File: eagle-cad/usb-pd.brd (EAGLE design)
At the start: 68.6 x 53.3 mm, 49 parts, among them Q1 CERAMIC_RESONATOR_SMD6M00G53Z, T1 FDN360P, U1 ATMEGA328-AU

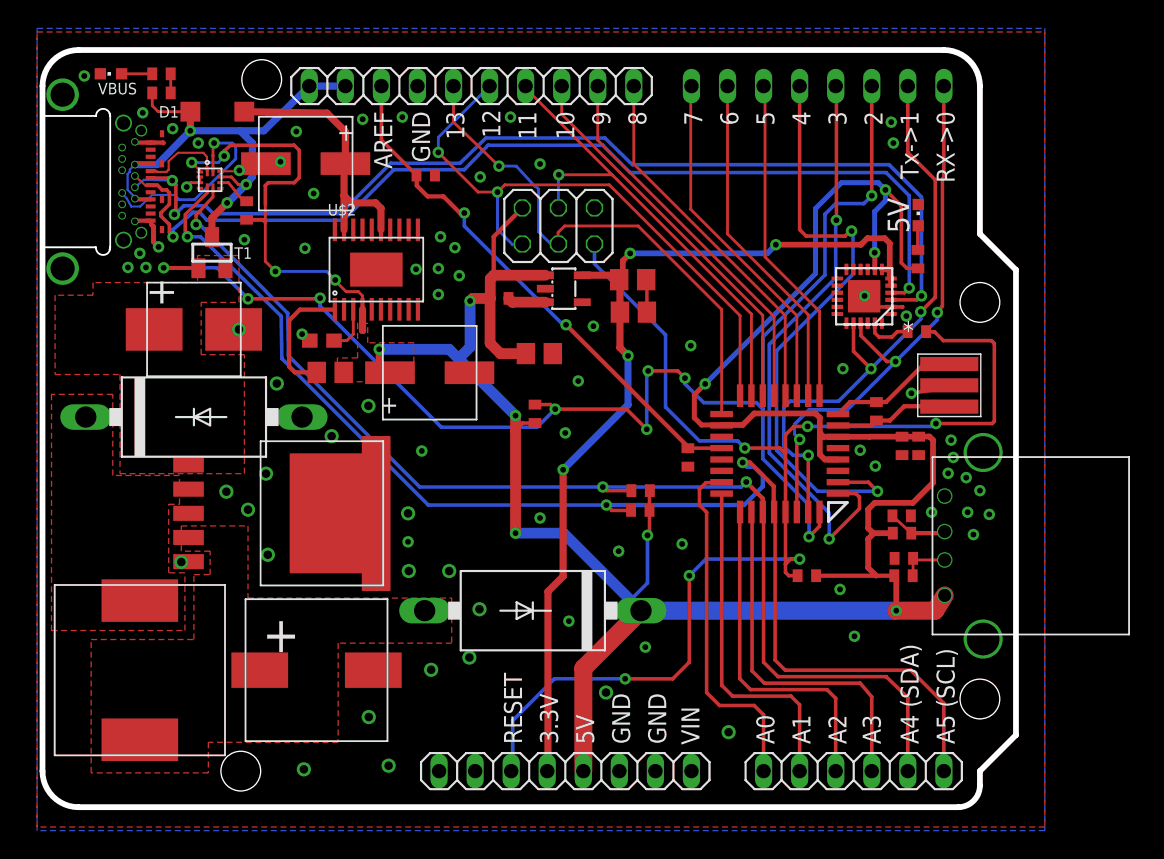
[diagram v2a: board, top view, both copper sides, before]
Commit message: Added new USB-C port, going to look at four-layer boards to get better Osh Park hole tolerances and ton of space for power planes
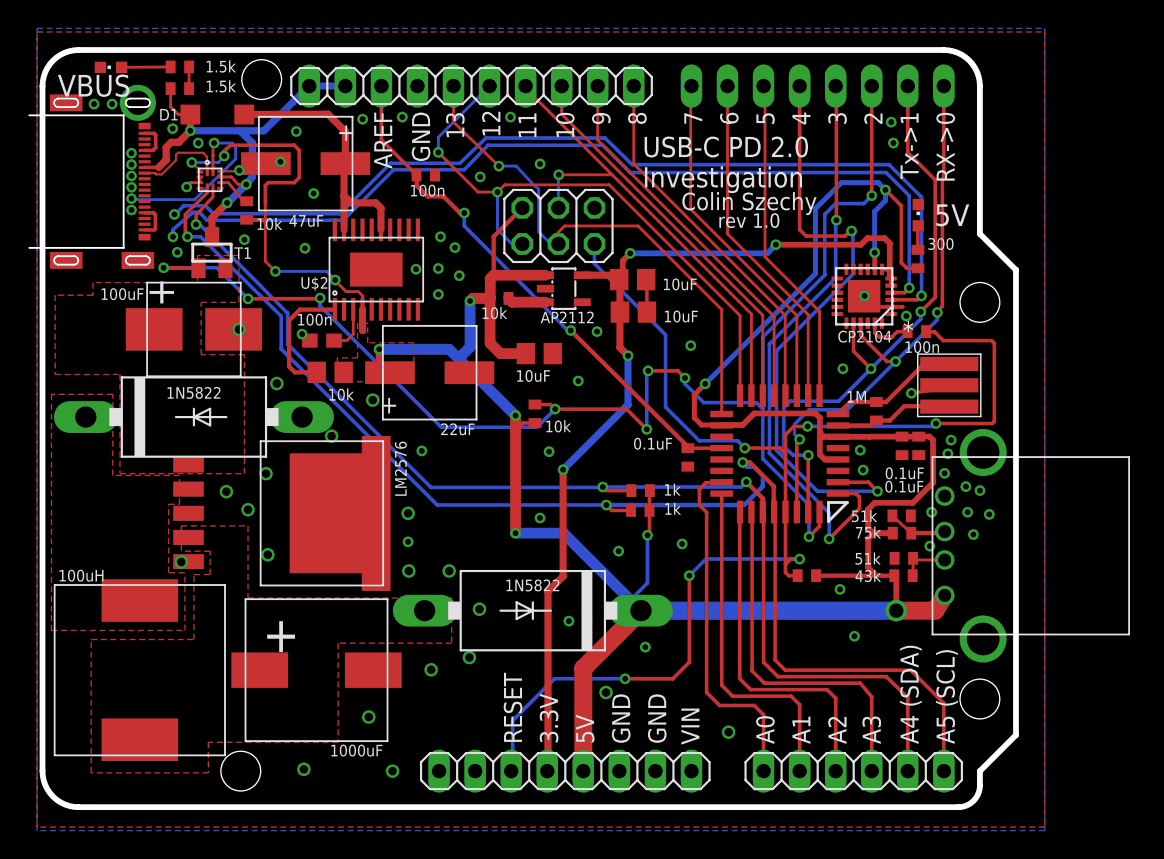
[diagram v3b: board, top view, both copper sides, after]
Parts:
- removed U$11: WURTH-865090543005-22uF, usb-pd:WURTH-865090543005
- removed U$6: TI-LM2576-5.0, usb-pd:TO-263
- removed U1: ATMEGA328-AU, usb-pd:32-TQFP
- added C11: AVE108M10G24T-F, usb-pd:AVE108M10G
- added J$1: TYPE-C-12401548E4, usb-pd:AMPHENOL-TYPE-C-12401548E4
- added J$2: UE27AC54100, usb-pd:UE27AC54100
- C13: value AVE108M10G24T-F -> WURTH-865090543005-22uF; device usb-pd:AVE108M10G -> usb-pd:WURTH-865090543005
- U$1: value TYPE-C-BR20-AK511 -> TI-LM2576-5.0; device usb-pd:TYPE-C-BR20-AK511 -> usb-pd:TO-263
- U$9: value UE27AC54100 -> ATMEGA328-AU; device usb-pd:UE27AC54100 -> usb-pd:32-TQFP
- moved U$1 23.5 mm to (10.3, 20.7), turned to 180 degrees
- moved C13 22.4 mm to (27.3, 30.6), turned to 180 degrees
- moved U$9 15.7 mm to (51.9, 24.9), turned to 180 degrees
- moved R9 1.38 mm to (9.68, 52.1)
- moved R8 1.33 mm to (9.68, 50.6)
- moved VBUS 0.46 mm to (4.83, 52.1)
- moved D1 0.20 mm to (12.3, 48.8)
- renumbered U$10 to C12, U$8 to C10
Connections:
- net +5V: now also C13.P$1, J$2.P$1, U$9.P$18, U$9.P$4, U$9.P$6; no longer U$11.P$1, U$9.P$1, U1.P$18, U1.P$4, U1.P$6
- net AD0: now also U$9.P$23; no longer U1.P$23
- net AD1: now also U$9.P$24; no longer U1.P$24
- net AD2: now also U$9.P$25; no longer U1.P$25
- net AD3: now also U$9.P$26; no longer U1.P$26
- net AREF: now also U$9.P$20; no longer U1.P$20
- net GND: now also C11.P$2, J$1.A1, J$1.A12, J$1.B1, J$1.B12, J$2.P$4, U$1.P$3, U$1.P$5, U$1.P$6, U$9.P$21, U$9.P$5; no longer U$1.A$1, U$1.A$12, U$1.B$1, U$1.B$12, U$11.P$2, U$6.P$3, U$6.P$5, U$6.P$6, U$9.P$4, U1.P$21, U1.P$5
- net IO2: now also U$9.P$32; no longer U1.P$32
- net IO3: now also U$9.P$1; no longer U1.P$1
- net IO4: now also U$9.P$2; no longer U1.P$2
- net IO5: now also U$9.P$9; no longer U1.P$9
- net IO6: now also U$9.P$10; no longer U1.P$10
- net IO7: now also U$9.P$11; no longer U1.P$11
- net IO8: now also U$9.P$12; no longer U1.P$12
- net IO9: now also U$9.P$13; no longer U1.P$13
- net MISO: now also U$9.P$16; no longer U1.P$16
- net MOSI: now also U$9.P$15; no longer U1.P$15
- net N$1: now also U$1.P$1; no longer U$6.P$1
- net N$15: now also C11.P$1, U$1.P$4; no longer C13.P$1, U$6.P$4
- net N$17: now also J$2.P$2; no longer U$9.P$2
- net N$18: now also J$2.P$3; no longer U$9.P$3
- net N$2: now also U$9.P$7; no longer U1.P$7
- net N$3: now also U$9.P$8; no longer U1.P$8
- net N$5: now also J$1.A5; no longer U$1.A$5
- net N$6: now also J$1.B5; no longer U$1.B$5
- net N$9: now also U$1.P$2; no longer U$6.P$2
- net PD_SCL: now also U$9.P$28; no longer U1.P$28
- net PD_SDA: now also U$9.P$27; no longer U1.P$27
- net RESET: now also U$9.P$29; no longer U1.P$29
- net SCLK: now also U$9.P$17; no longer U1.P$17
- net SS: now also U$9.P$14; no longer U1.P$14
- net USB+: now also J$1.A6, J$1.B6; no longer U$1.A$6, U$1.B$6
- net USB-: now also J$1.A7, J$1.B7; no longer U$1.A$7, U$1.B$7
- net USB_RX: now also U$9.P$30; no longer U1.P$30
- net USB_TX: now also U$9.P$31; no longer U1.P$31
- net VBUS: now also J$1.A4, J$1.A9, J$1.B4, J$1.B9; no longer U$1.A$4, U$1.A$9, U$1.B$4, U$1.B$9
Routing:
- net USB+: track 73.1 -> 66.2 mm, vias 3 -> 2
- net USB-: track 71.3 -> 64.7 mm
- net VBUS: track 38.6 -> 32.5 mm
- net N$6: track 14.7 -> 13.1 mm
- net N$11: track 2.16 -> 3.45 mm
- net N$18: track 4.77 -> 4.20 mm
- net GND: track 22.1 -> 22.0 mm, vias 77 -> 75
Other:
- board text added: "1000uF"
- board text added: "100uF"
- board text added: "100uH"
- board text added: "1N5822"
- board text added: "22uF"
- board text added: "47uF"
- board text added: "AP2112"
- board text added: "CP2104"
- board text added: "Colin Szechy"
- board text added: "LM2576"
- board text added: "USB-C PD 2.0 Investigation"
- board text added: "rev 1.0"
